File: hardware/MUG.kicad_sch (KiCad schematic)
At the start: 8 parts, among them Q5 S8050, SW1 SW_SPST, U5 STM32F103C8Tx

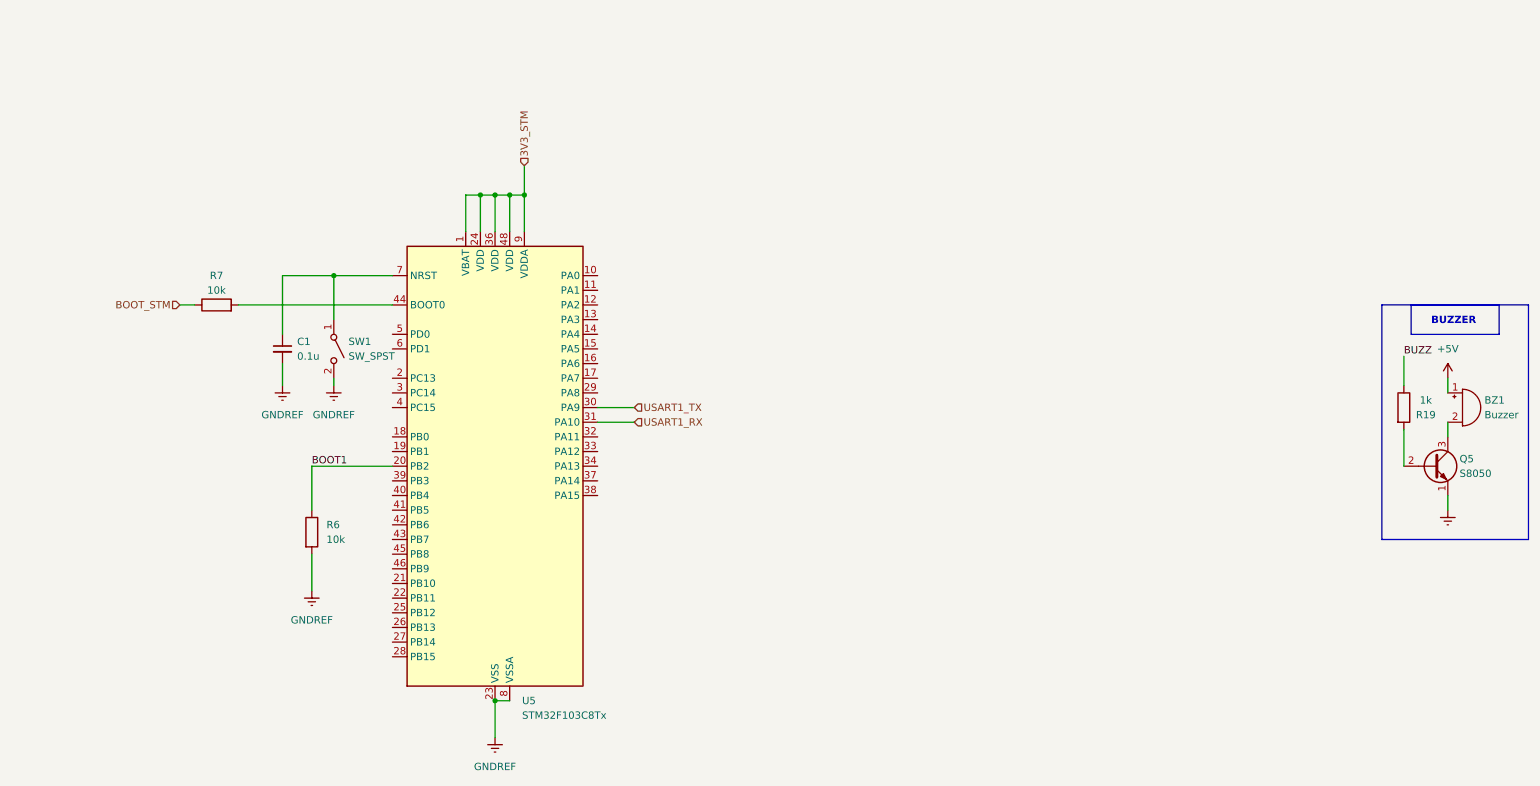
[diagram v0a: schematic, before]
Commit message: mvp
features:
	Logic Power Supply
	Safety Relay
	Main Unit
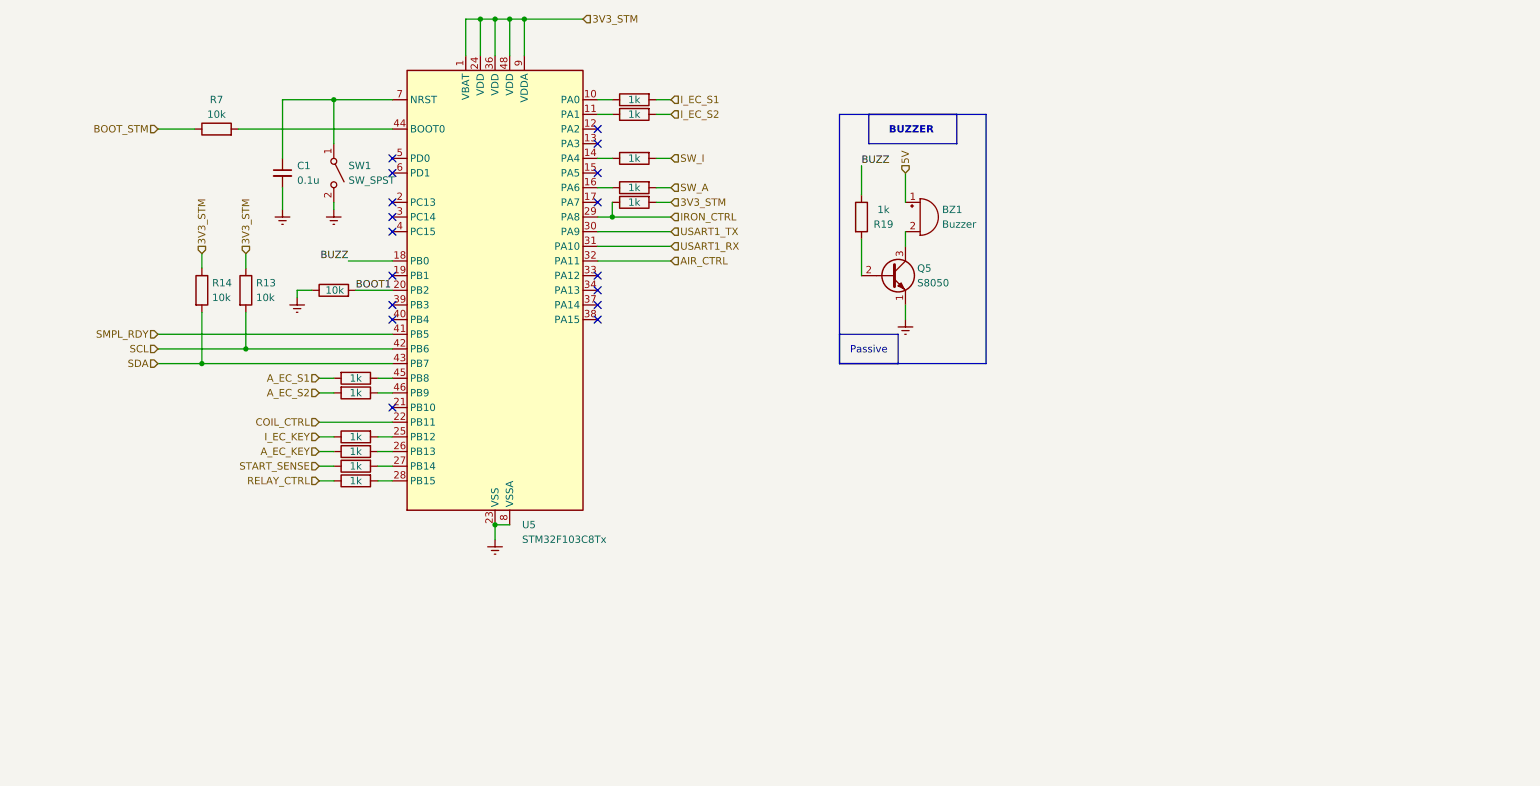
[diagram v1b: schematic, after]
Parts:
- added R12, R15, R17, R18, R29, R30, R31, R32, R33, R34, R35: 1k, symbol Device:R
- added R13, R14: 10k, symbol Device:R
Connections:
- net 3V3_STM: now also R13.1, R14.1, R15.2
- net BOOT1: now also R6.2; no longer R6.1
- net BUZZ: now also U5.18 (PB0)
- net GNDREF: now also R6.1; no longer R6.2
- net at U5.10 (PA0): now also R17.1
- net at U5.11 (PA1): now also R18.1
- net at U5.14 (PA4): now also R35.1
- net at U5.16 (PA6): now also R34.1
- net COIL_CTRL: now reaches U5.22 (PB11)
- net at U5.25 (PB12): now also R29.2
- net at U5.26 (PB13): now also R30.2
- net at U5.27 (PB14): now also R12.2
- net at U5.28 (PB15): now also R33.2
- net IRON_CTRL: now reaches U5.29 (PA8)
- net IRON_CTRL: now also R15.1
- net AIR_CTRL: now reaches U5.32 (PA11)
- net SMPL_RDY: now reaches U5.41 (PB5)
- net SCL: now reaches U5.42 (PB6)
- net SCL: now also R13.2
- net SDA: now reaches U5.43 (PB7)
- net SDA: now also R14.2
- net at U5.45 (PB8): now also R31.1
- net at U5.46 (PB9): now also R32.1
- net +5V renamed 5V
- new net A_EC_KEY: R30.1
- new net A_EC_S1: R31.2
- new net A_EC_S2: R32.2
- new net I_EC_KEY: R29.1
- new net I_EC_S1: R17.2
- new net I_EC_S2: R18.2
- new net RELAY_CTRL: R33.1
- new net START_SENSE: R12.1
- new net SW_A: R34.2
- new net SW_I: R35.2
- no-connect marks 0 -> 17
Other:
- note added: "Passive"
- moved on the sheet: BZ1, C1, Q5, R19, R7, SW1, U5

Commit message: starting pcb
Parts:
- added C10, C9: 22pF, Capacitor_SMD:C_0603_1608Metric, symbol Device:C_Small
- added C16, C17, C18, C19, C20: 0.1u, Capacitor_SMD:C_0603_1608Metric, symbol Device:C_Small
- added R36, R37: 10k, Resistor_SMD:R_0603_1608Metric, symbol Device:R
- added Y2: Crystal_GND24_Small, Crystal:Crystal_SMD_3225-4Pin_3.2x2.5mm, symbol Device:Crystal_GND24_Small
- BZ1: footprint (none) -> Buzzer_Beeper:Buzzer_12x9.5RM7.6
- C1: footprint (none) -> Capacitor_SMD:C_0603_1608Metric
- Q5: footprint Package_TO_SOT_THT:TO-92_Inline -> Package_TO_SOT_SMD:SOT-23-3
- R12, R13, R14, R15, R17, R18, R19, R29, R30, R31, R32, R33, R34, R35, R6, R7: footprint (none) -> Resistor_SMD:R_0603_1608Metric
- SW1: footprint (none) -> Button_Switch_THT:SW_PUSH_6mm_H8mm
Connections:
- net 3V3_STM: now also C16.1, C17.1, C18.1, C19.1, C20.1, R36.2
- net GNDREF: now also C10.2, C16.2, C17.2, C18.2, C19.2, C20.2, C9.2, R37.2, Y2.2, Y2.4
- net SWDIO: now reaches U5.34 (PA13)
- net SWDIO: now also R36.1
- net SWCLK: now reaches U5.37 (PA14)
- net SWCLK: now also R37.1
- net at U5.5 (PD0): now also C10.1, Y2.1
- net at U5.6 (PD1): now also C9.1, Y2.3
- no-connect marks 17 -> 13
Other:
- moved on the sheet: BZ1, C1, Q5, R13, R14, R19, R7, SW1

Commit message: pcb mvp
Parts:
- SW1: footprint Button_Switch_THT:SW_PUSH_6mm_H8mm -> Button_Switch_THT:SW_PUSH_4.5mm
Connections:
- net at C10.1, U5.5 (PD0): now also Y2.3; no longer Y2.1
- net at C9.1, U5.6 (PD1): now also Y2.1; no longer Y2.3

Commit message: last
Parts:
- removed Y2: Crystal_GND24_Small, Crystal:Crystal_SMD_3225-4Pin_3.2x2.5mm, symbol Device:Crystal_GND24_Small
- added R41, R42: 1k, Resistor_SMD:R_0805_2012Metric_Pad1.20x1.40mm_HandSolder, symbol Device:R
- added Y1: X50328MSB2GI, Crystal:Crystal_SMD_5032-2Pin_5.0x3.2mm, symbol Device:Crystal
- C1, C16, C17, C18, C19, C20: footprint Capacitor_SMD:C_0603_1608Metric -> Capacitor_SMD:C_0805_2012Metric_Pad1.18x1.45mm_HandSolder; LCSC (none) -> C14663
- C10, C9: footprint Capacitor_SMD:C_0603_1608Metric -> Capacitor_SMD:C_0805_2012Metric_Pad1.18x1.45mm_HandSolder; LCSC (none) -> C1653
- Q5: value S8050 -> 2N2222; footprint Package_TO_SOT_SMD:SOT-23-3 -> Package_TO_SOT_THT:TO-92_Inline; LCSC (none) -> C2146
- R12, R15, R17, R18, R19, R29, R30, R31, R32, R33, R34, R35: footprint Resistor_SMD:R_0603_1608Metric -> Resistor_SMD:R_0805_2012Metric_Pad1.20x1.40mm_HandSolder; LCSC (none) -> C21190
- R13, R14, R36, R37, R6, R7: footprint Resistor_SMD:R_0603_1608Metric -> Resistor_SMD:R_0805_2012Metric_Pad1.20x1.40mm_HandSolder; LCSC (none) -> C25804
- SW1: footprint Button_Switch_THT:SW_PUSH_4.5mm -> Button_Switch_THT:SW_PUSH_6mm_H8mm
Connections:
- net USART1_RX: now also R42.2; no longer U5.31 (PA10)
- net USART1_TX: now also R41.2; no longer U5.30 (PA9)
- net at C9.1, U5.6 (PD1): now also Y1.2
- net at C10.1, U5.5 (PD0): now also Y1.1
- new net: R41.1, U5.30 (PA9)
- new net: R42.1, U5.31 (PA10)
